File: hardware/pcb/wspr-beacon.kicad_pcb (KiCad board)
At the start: 2 copper layers, 100 x 100 mm, 70 parts, among them J1 USB_OTG, J2 Conn_01x04, J3 Conn_02x03_Odd_Even, J4 Conn_Coaxial, J5 Conn_Coaxial, J6 Conn_Coaxial, U1 AP1117-33, U2 ATMEGA328-AU, U3 Si5351A, X1 ASE-25MHz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

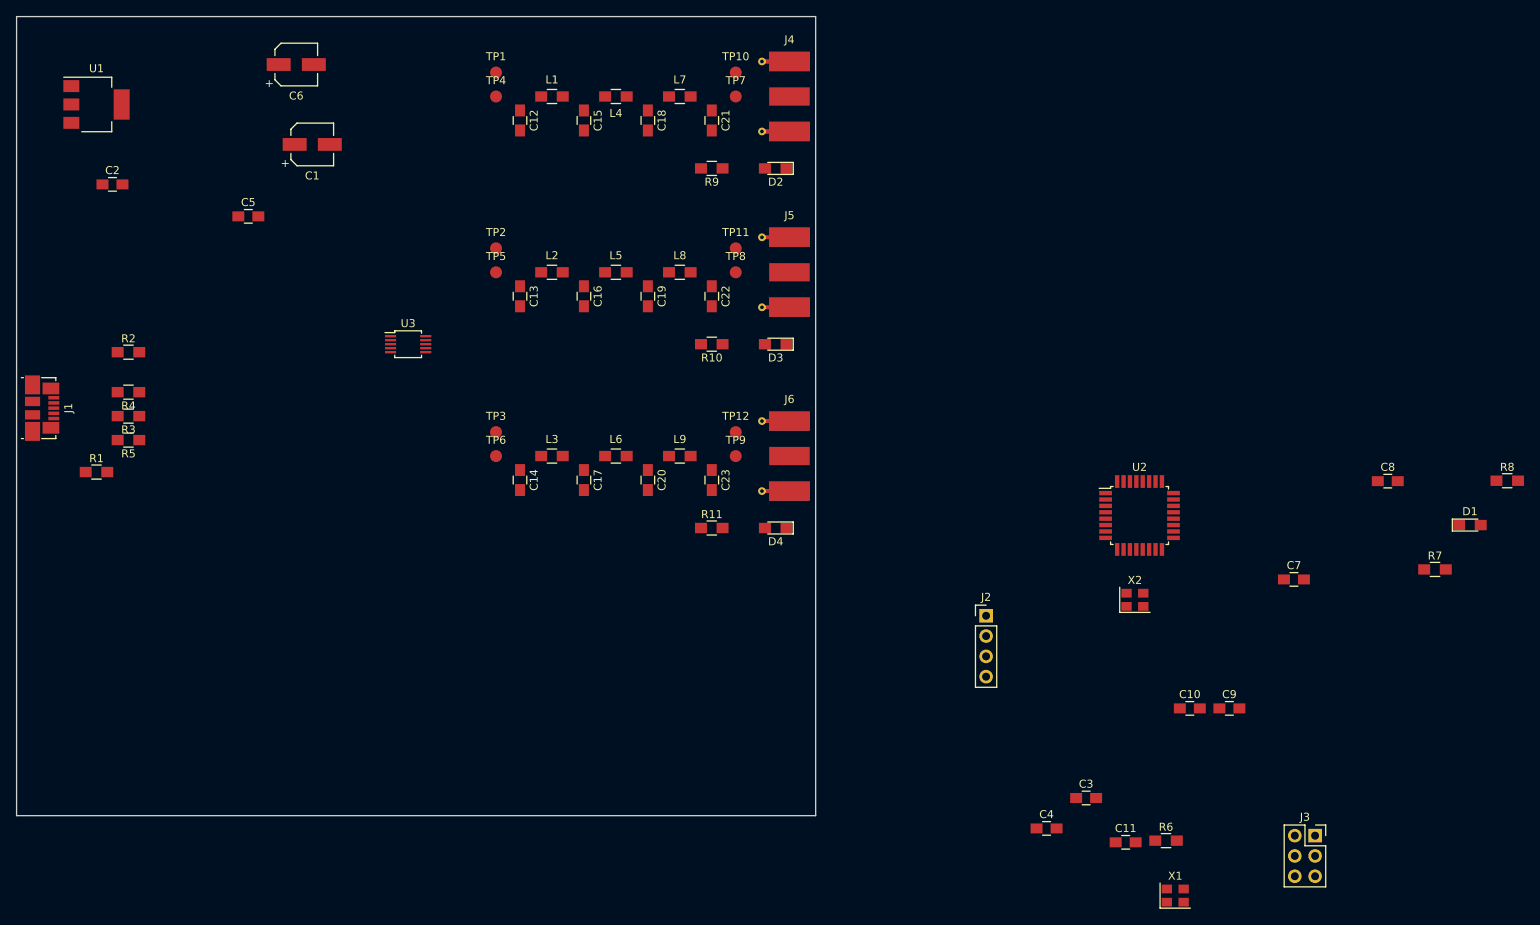
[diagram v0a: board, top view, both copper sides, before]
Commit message: Continue with layout and add pull-ups for I2C
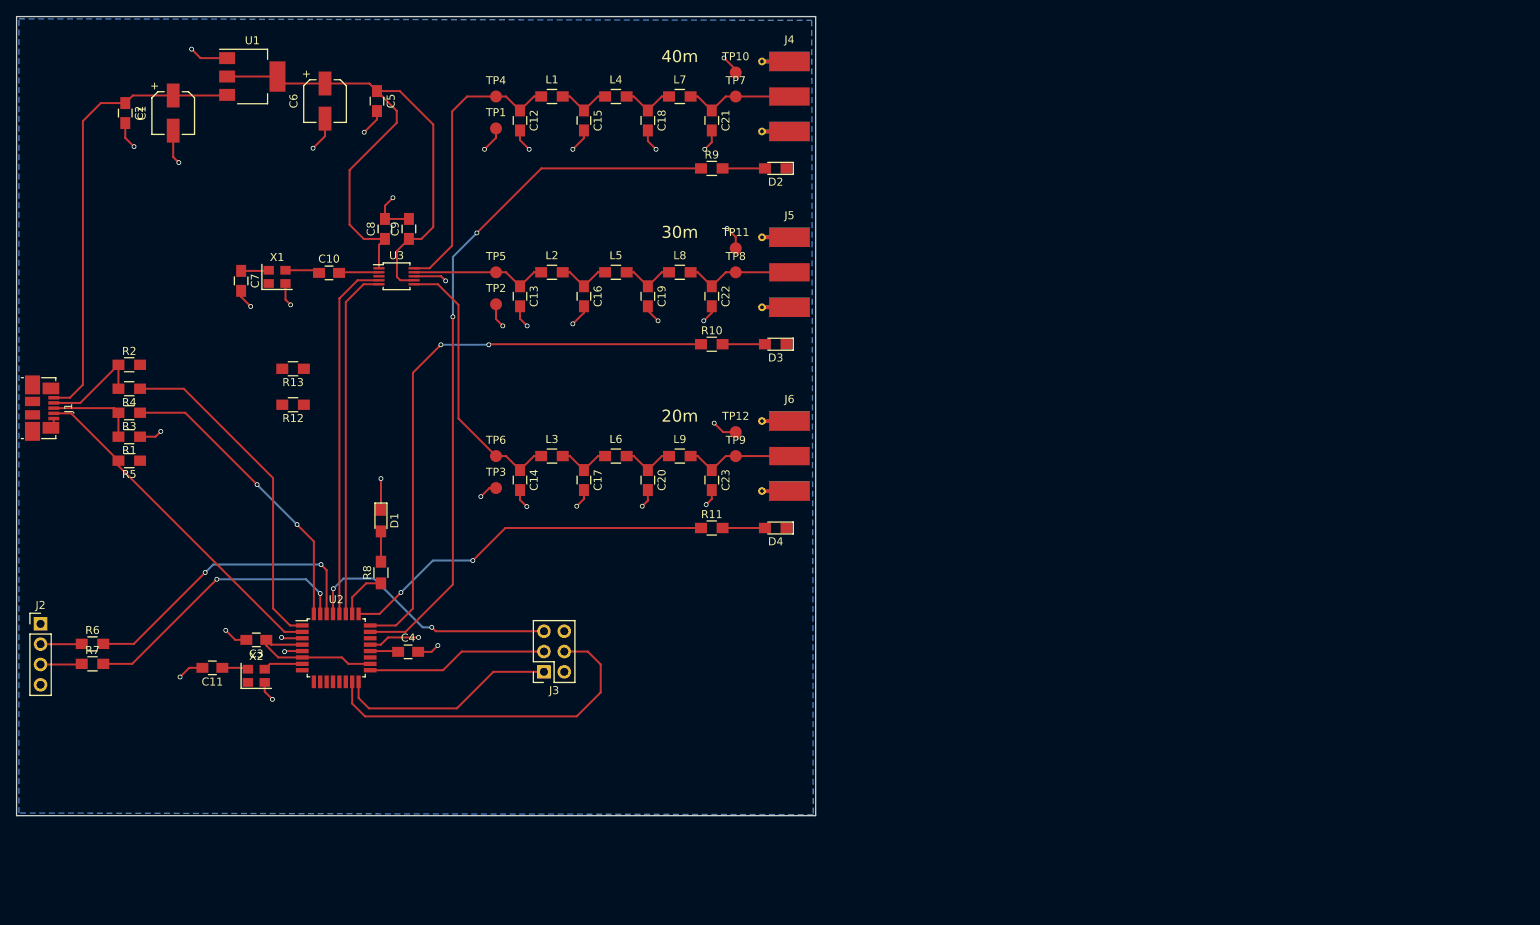
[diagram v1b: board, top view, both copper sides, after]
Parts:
- added R12: 4k7, Resistors_SMD:R_0805_HandSoldering, F.Cu at (84.6, 98.6)
- added R13: 4k7, Resistors_SMD:R_0805_HandSoldering, F.Cu at (84.6, 94.1)
- moved R7 168.4 mm to (59.5, 131.0)
- moved R8 141.4 mm to (95.6, 119.6), turned to 90 degrees
- moved C7 136.9 mm to (78.1, 83.1), turned to 270 degrees
- moved R6 136.6 mm to (59.5, 128.5)
- moved X1 136.5 mm to (82.6, 82.6)
- moved D1 136.3 mm to (95.6, 113.1), turned to 270 degrees
- moved C8 129.4 mm to (96.1, 76.6), turned to 90 degrees
- moved C10 120.7 mm to (89.1, 82.1)
- moved C9 118.9 mm to (99.1, 76.6), turned to 90 degrees
- moved J2 118.3 mm to (53.0, 126.0)
- moved C11 116.4 mm to (74.5, 131.5), turned to 180 degrees
- moved X2 110.4 mm to (80.0, 132.5)
- moved C3 105.7 mm to (80.0, 128.0), turned to 180 degrees
- moved U2 101.9 mm to (90.0, 129.0)
- moved J3 98.7 mm to (116.0, 132.0), turned to 180 degrees
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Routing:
- net GND: track 0.00 -> 115.3 mm, vias 0 -> 36
- net +3V3: track 0.00 -> 108.0 mm
- net /LED_CLK0: track 0.00 -> 89.4 mm, vias 0 -> 2
- net /LED_CLK1: track 0.00 -> 73.3 mm, vias 0 -> 2
- net VBUS: track 0.00 -> 56.7 mm
- net /LED_CLK2: track 0.00 -> 47.3 mm, vias 0 -> 2
- net /SCL: track 0.00 -> 45.4 mm
- net /MOSI: track 0.00 -> 44.5 mm
- net /SDA: track 0.00 -> 44.1 mm
- net /ID: track 0.00 -> 42.8 mm
- net /D-: track 0.00 -> 42.1 mm
- net Net-(R6-Pad2): track 0.00 -> 37.8 mm, vias 0 -> 2
- net /D+: track 0.00 -> 37.5 mm, vias 0 -> 2
- net Net-(C12-Pad1): track 0.00 -> 36.1 mm
- net Net-(R7-Pad2): track 0.00 -> 34.8 mm, vias 0 -> 2
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- added copper zone on B.Cu, net GND
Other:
- board text added: "20m"
- board text added: "30m"
- board text added: "40m"

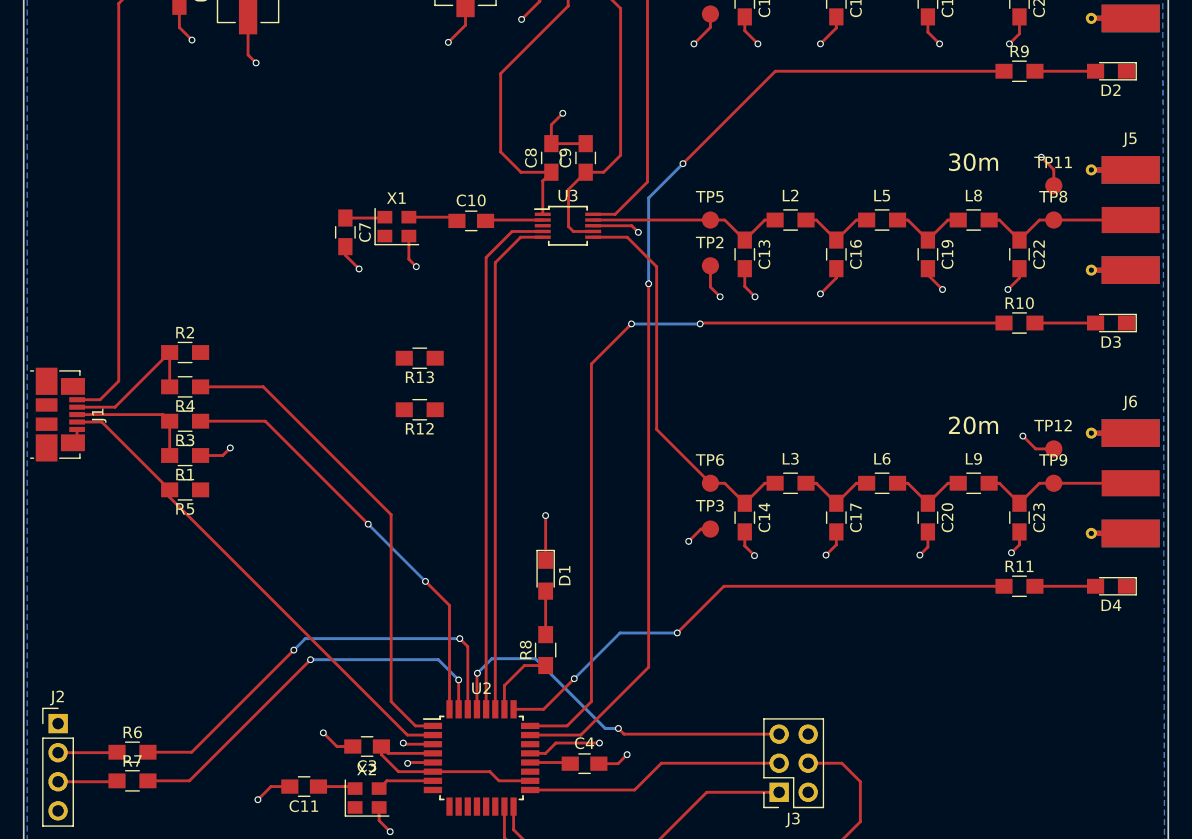
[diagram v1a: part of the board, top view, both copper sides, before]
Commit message: Add reset button
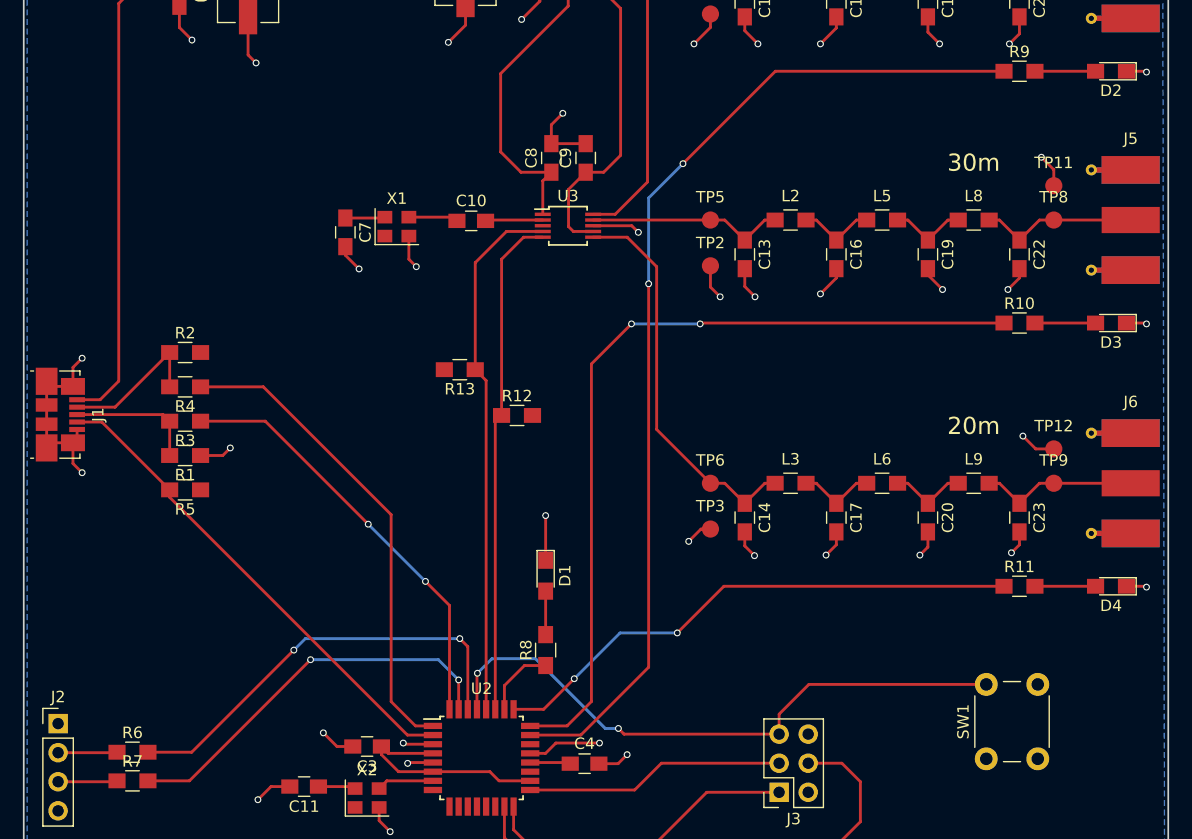
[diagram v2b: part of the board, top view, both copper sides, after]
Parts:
- added SW1: SW_Push, Buttons_Switches_THT:SW_PUSH_6mm, F.Cu at (134.1, 129.1)
- moved R12 8.51 mm to (93.1, 99.1), turned to 0 degrees
- moved R13 3.64 mm to (88.1, 95.1)
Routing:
- net GND: track 115.3 -> 137.1 mm, vias 36 -> 41
- net /RESET: track 32.8 -> 53.7 mm
- net /SCL: track 45.4 -> 46.4 mm
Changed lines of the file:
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@@
 (kicad_pcb (version 4) (host pcbnew 4.0.7)
   (general
-    (links 164)
-    (no_connects 32)
+    (links 168)
+    (no_connects 22)
     (area 49.924999 49.924999 150.075001 150.075001)
     (thickness 1.6)
     (drawings 7)
-    (tracks 332)
+    (tracks 361)
     (zones 0)
-    (modules 72)
+    (modules 73)
     (nets 55)
   )
@@
   )
   (module Resistors_SMD:R_0805_HandSoldering (layer F.Cu)
-    (at 84.6 98.575 180)
+    (at 93.1 99.075)
     (descr "Resistor SMD 0805, hand soldering")
     (tags "resistor 0805")
     (attr smd)
-    (fp_text reference R12 (at 0 -1.7 180) (layer F.SilkS)
+    (fp_text reference R12 (at 0 -1.7) (layer F.SilkS)
       (effects (font (size 1 1) (thickness 0.15)))
     )
-    (fp_text value 4k7 (at 0 1.75 180) (layer F.Fab)
+    (fp_text value 4k7 (at 0 1.75) (layer F.Fab)
       (effects (font (size 1 1) (thickness 0.15)))
     )
-    (fp_text user %R (at 0 0 180) (layer F.Fab)
+    (fp_text user %R (at 0 0) (layer F.Fab)
       (effects (font (size 0.5 0.5) (thickness 0.075)))
     )
@@
     (fp_line (start 2.35 0.9) (end 2.35 -0.9) (layer F.CrtYd) (width 0.05))
     (fp_line (start 2.35 0.9) (end -2.35 0.9) (layer F.CrtYd) (width 0.05))
-    (pad 1 smd rect (at -1.35 0 180) (size 1.5 1.3) (layers F.Cu F.Paste F.Mask)
+    (pad 1 smd rect (at -1.35 0) (size 1.5 1.3) (layers F.Cu F.Paste F.Mask)
       (net 50 /SDA))
-    (pad 2 smd rect (at 1.35 0 180) (size 1.5 1.3) (layers F.Cu F.Paste F.Mask)
+    (pad 2 smd rect (at 1.35 0) (size 1.5 1.3) (layers F.Cu F.Paste F.Mask)
       (net 3 +3V3))
     (model ${KISYS3DMOD}/Resistors_SMD.3dshapes/R_0805.wrl
@@
   )
   (module Resistors_SMD:R_0805_HandSoldering (layer F.Cu)
-    (at 84.6 94.075 180)
+    (at 88.1 95.075 180)
     (descr "Resistor SMD 0805, hand soldering")
     (tags "resistor 0805")
@@
     )
   )
+  (module Buttons_Switches_THT:SW_PUSH_6mm (layer F.Cu)
+    (at 134.1 129.075 90)
+    (descr https://www.omron.com/ecb/products/pdf/en-b3f.pdf)
+    (tags "tact sw push 6mm")
+    (fp_text reference SW1 (at 3.25 -2 90) (layer F.SilkS)
+      (effects (font (size 1 1) (thickness 0.15)))
+    )
+    (fp_text value SW_Push (at 3.75 6.7 90) (layer F.Fab)
+      (effects (font (size 1 1) (thickness 0.15)))
+    )
+    (fp_text user %R (at 3.25 2.25 90) (layer F.Fab)
+      (effects (font (size 1 1) (thickness 0.15)))
+    )
+    (fp_line (start 3.25 -0.75) (end 6.25 -0.75) (layer F.Fab) (width 0.1))
+    (fp_line (start 6.25 -0.75) (end 6.25 5.25) (layer F.Fab) (width 0.1))
+    (fp_line (start 6.25 5.25) (end 0.25 5.25) (layer F.Fab) (width 0.1))
+    (fp_line (start 0.25 5.25) (end 0.25 -0.75) (layer F.Fab) (width 0.1))
+    (fp_line (start 0.25 -0.75) (end 3.25 -0.75) (layer F.Fab) (width 0.1))
+    (fp_line (start 7.75 6) (end 8 6) (layer F.CrtYd) (width 0.05))
+    (fp_line (start 8 6) (end 8 5.75) (layer F.CrtYd) (width 0.05))
+    (fp_line (start 7.75 -1.5) (end 8 -1.5) (layer F.CrtYd) (width 0.05))
+    (fp_line (start 8 -1.5) (end 8 -1.25) (layer F.CrtYd) (width 0.05))
+    (fp_line (start -1.5 -1.25) (end -1.5 -1.5) (layer F.CrtYd) (width 0.05))
+    (fp_line (start -1.5 -1.5) (end -1.25 -1.5) (layer F.CrtYd) (width 0.05))
+    (fp_line (start -1.5 5.75) (end -1.5 6) (layer F.CrtYd) (width 0.05))
+    (fp_line (start -1.5 6) (end -1.25 6) (layer F.CrtYd) (width 0.05))
+    (fp_line (start -1.25 -1.5) (end 7.75 -1.5) (layer F.CrtYd) (width 0.05))
+    (fp_line (start -1.5 5.75) (end -1.5 -1.25) (layer F.CrtYd) (width 0.05))
+    (fp_line (start 7.75 6) (end -1.25 6) (layer F.CrtYd) (width 0.05))
+    (fp_line (start 8 -1.25) (end 8 5.75) (layer F.CrtYd) (width 0.05))
+    (fp_line (start 1 5.5) (end 5.5 5.5) (layer F.SilkS) (width 0.12))
+    (fp_line (start -0.25 1.5) (end -0.25 3) (layer F.SilkS) (width 0.12))
+    (fp_line (start 5.5 -1) (end 1 -1) (layer F.SilkS) (width 0.12))
+    (fp_line (start 6.75 3) (end 6.75 1.5) (layer F.SilkS) (width 0.12))
+    (fp_circle (center 3.25 2.25) (end 1.25 2.5) (layer F.Fab) (width 0.1))
+    (pad 2 thru_hole circle (at 0 4.5 180) (size 2 2) (drill 1.1) (layers *.Cu *.Mask)
+      (net 2 GND))
+    (pad 1 thru_hole circle (at 0 0 180) (size 2 2) (drill 1.1) (layers *.Cu *.Mask)
+      (net 35 /RESET))
+    (pad 2 thru_hole circle (at 6.5 4.5 180) (size 2 2) (drill 1.1) (layers *.Cu *.Mask)
+      (net 2 GND))
+    (pad 1 thru_hole circle (at 6.5 0 180) (size 2 2) (drill 1.1) (layers *.Cu *.Mask)
+      (net 35 /RESET))
+    (model ${KISYS3DMOD}/Buttons_Switches_THT.3dshapes/SW_PUSH_6mm.wrl
+      (at (xyz 0.005 0 0))
+      (scale (xyz 0.3937 0.3937 0.3937))
+      (rotate (xyz 0 0 0))
+    )
+  )
   (gr_text 20m (at 133 100) (layer F.SilkS)
     (effects (font (size 1.5 1.5) (thickness 0.3)))
@@
   (segment (start 69.6 59.875) (end 76.275 59.875) (width 0.25) (layer F.Cu) (net 1))
   (segment (start 76.275 59.875) (end 76.35 59.8) (width 0.25) (layer F.Cu) (net 1))
+  (segment (start 54.3 96.5375) (end 54.3 94.875) (width 0.25) (layer F.Cu) (net 2))
+  (via (at 55.1 94.075) (size 0.6) (drill 0.4) (layers F.Cu B.Cu) (net 2))
+  (segment (start 54.3 94.875) (end 55.1 94.075) (width 0.25) (layer F.Cu) (net 2))
+  (segment (start 54.3 101.4625) (end 52.4475 101.4625) (width 0.25) (layer F.Cu) (net 2))
+  (segment (start 52.4475 101.4625) (end 52 101.91) (width 0.25) (layer F.Cu) (net 2))
+  (segment (start 52 99.84) (end 52 101.91) (width 0.25) (layer F.Cu) (net 2))
+  (segment (start 52 98.16) (end 52 99.84) (width 0.25) (layer F.Cu) (net 2))
+  (segment (start 52 96.09) (end 52 98.16) (width 0.25) (layer F.Cu) (net 2))
+  (segment (start 54.3 96.5375) (end 52.4475 96.5375) (width 0.25) (layer F.Cu) (net 2))
+  (segment (start 52.4475 96.5375) (end 52 96.09) (width 0.25) (layer F.Cu) (net 2))
+  (segment (start 54.3 101.4625) (end 54.3 103.275) (width 0.25) (layer F.Cu) (net 2))
+  (via (at 55.1 104.075) (size 0.6) (drill 0.4) (layers F.Cu B.Cu) (net 2))
+  (segment (start 54.3 103.275) (end 55.1 104.075) (width 0.25) (layer F.Cu) (net 2))
+  (segment (start 146.35 69) (end 148.025 69) (width 0.25) (layer F.Cu) (net 2))
+  (via (at 148.1 69.075) (size 0.6) (drill 0.4) (layers F.Cu B.Cu) (net 2))
+  (segment (start 148.025 69) (end 148.1 69.075) (width 0.25) (layer F.Cu) (net 2))
+  (segment (start 146.35 114) (end 148.025 114) (width 0.25) (layer F.Cu) (net 2) (status 10))
+  (via (at 148.1 114.075) (size 0.6) (drill 0.4) (layers F.Cu B.Cu) (net 2))
+  (segment (start 148.025 114) (end 148.1 114.075) (width 0.25) (layer F.Cu) (net 2))
+  (segment (start 146.35 91) (end 148.025 91) (width 0.25) (layer F.Cu) (net 2))
+  (via (at 148.1 91.075) (size 0.6) (drill 0.4) (layers F.Cu B.Cu) (net 2))
+  (segment (start 148.025 91) (end 148.1 91.075) (width 0.25) (layer F.Cu) (net 2))
   (segment (start 85.75 129.4) (end 83.616 129.4) (width 0.25) (layer F.Cu) (net 2))
   (via (at 83.542 129.474) (size 0.6) (drill 0.4) (layers F.Cu B.Cu) (net 2))
@@
   (via (at 98.1 122.075) (size 0.6) (drill 0.4) (layers F.Cu B.Cu) (net 25))
   (segment (start 95.425 124.75) (end 98.1 122.075) (width 0.25) (layer F.Cu) (net 25))
-  (segment (start 138.35 114) (end 143.65 114) (width 0.25) (layer F.Cu) (net 26))
+  (segment (start 138.35 114) (end 143.65 114) (width 0.25) (layer F.Cu) (net 26) (status 20))
   (segment (start 54.66 98.35) (end 57.975 98.35) (width 0.25) (layer F.Cu) (net 27))
   (segment (start 57.975 98.35) (end 62.75 93.575) (width 0.25) (layer F.Cu) (net 27))
@@
   (segment (start 123.1 131.075) (end 123.1 134.575) (width 0.25) (layer F.Cu) (net 34))
   (segment (start 121.485 129.46) (end 123.1 131.075) (width 0.25) (layer F.Cu) (net 34))
+  (segment (start 116 126.92) (end 116 125.175) (width 0.25) (layer F.Cu) (net 35))
+  (segment (start 118.6 122.575) (end 134.1 122.575) (width 0.25) (layer F.Cu) (net 35) (status 20))
+  (segment (start 116 125.175) (end 118.6 122.575) (width 0.25) (layer F.Cu) (net 35))
   (segment (start 89.6 124.75) (end 89.6 121.638) (width 0.25) (layer F.Cu) (net 35))
   (segment (start 102.451 126.92) (end 116 126.92) (width 0.25) (layer F.Cu) (net 35))
@@
   (segment (start 85.75 131) (end 81.725 131) (width 0.25) (layer F.Cu) (net 40))
   (segment (start 81.725 131) (end 81.05 131.675) (width 0.25) (layer F.Cu) (net 40))
-  (segment (start 91.2 124.75) (end 91.2 85.725) (width 0.25) (layer F.Cu) (net 50) (status 400000))
-  (segment (start 93.425 83.5) (end 95.35 83.5) (width 0.25) (layer F.Cu) (net 50) (status 800000))
-  (segment (start 91.2 85.725) (end 93.425 83.5) (width 0.25) (layer F.Cu) (net 50))
-  (segment (start 90.4 124.75) (end 90.4 85.275) (width 0.25) (layer F.Cu) (net 51) (status 400000))
-  (segment (start 92.675 83) (end 95.35 83) (width 0.25) (layer F.Cu) (net 51) (status 800000))
-  (segment (start 90.4 85.275) (end 92.675 83) (width 0.25) (layer F.Cu) (net 51))
+  (segment (start 91.75 99.075) (end 91.75 85.425) (width 0.25) (layer F.Cu) (net 50))
+  (segment (start 93.675 83.5) (end 95.35 83.5) (width 0.25) (layer F.Cu) (net 50))
+  (segment (start 91.75 85.425) (end 93.675 83.5) (width 0.25) (layer F.Cu) (net 50))
+  (segment (start 91.2 124.75) (end 91.2 99.625) (width 0.25) (layer F.Cu) (net 50))
+  (segment (start 91.2 99.625) (end 91.75 99.075) (width 0.25) (layer F.Cu) (net 50))
+  (segment (start 89.45 95.075) (end 89.45 85.725) (width 0.25) (layer F.Cu) (net 51))
+  (segment (start 92.175 83) (end 95.35 83) (width 0.25) (layer F.Cu) (net 51))
+  (segment (start 89.45 85.725) (end 92.175 83) (width 0.25) (layer F.Cu) (net 51))
+  (segment (start 90.4 124.75) (end 90.4 96.025) (width 0.25) (layer F.Cu) (net 51))
+  (segment (start 90.4 96.025) (end 89.45 95.075) (width 0.25) (layer F.Cu) (net 51))
   (zone (net 2) (net_name GND) (layer B.Cu) (hatch edge 0.508)
     (connect_pads (clearance 0.508))
